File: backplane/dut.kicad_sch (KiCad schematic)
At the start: 1 part, among them J1 Conn_02x06_Odd_Even

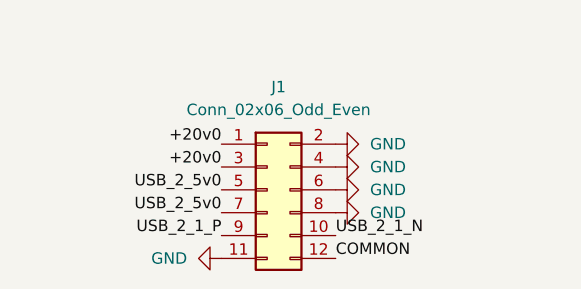
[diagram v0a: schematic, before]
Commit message: Add 20V -> 3V3 buck
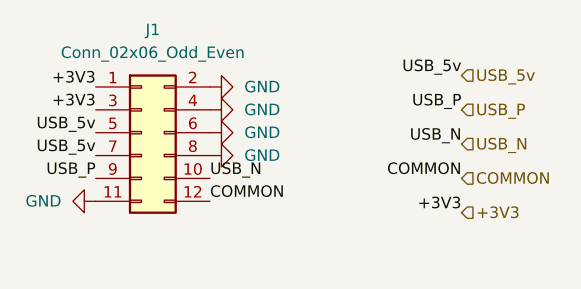
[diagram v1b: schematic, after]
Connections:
- net +20v0 renamed +3V3
- net USB_2_1_N renamed USB_N
- net USB_2_1_P renamed USB_P
- net USB_2_5v0 renamed USB_5v
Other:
- moved on the sheet: J1

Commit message: More work on the backplane
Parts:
- removed J1: Conn_02x06_Odd_Even, Connector_IDC:IDC-Header_2x06_P2.54mm_Vertical, symbol Connector_Generic:Conn_02x06_Odd_Even
- added J1: Conn_02x03_Odd_Even, Connector_IDC:IDC-Header_2x03_P2.54mm_Vertical_SMD, symbol Connector_Generic:Conn_02x03_Odd_Even
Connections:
- net +3V3: now also J1.1 (Pin_1)
- net GND: now also J1.2 (Pin_2)
- net USB_5v: now also J1.3 (Pin_3)
- net USB_N: now also J1.6 (Pin_6)
- net USB_P: now also J1.5 (Pin_5)
- new net PRESENT: J1.4 (Pin_4)
